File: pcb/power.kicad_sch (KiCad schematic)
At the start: 33 parts, among them J1 USB_C_PowerOnly_6P, J2 Power, J3 Power, U1 AZ1084-3.3, U2 LM66200DRLR

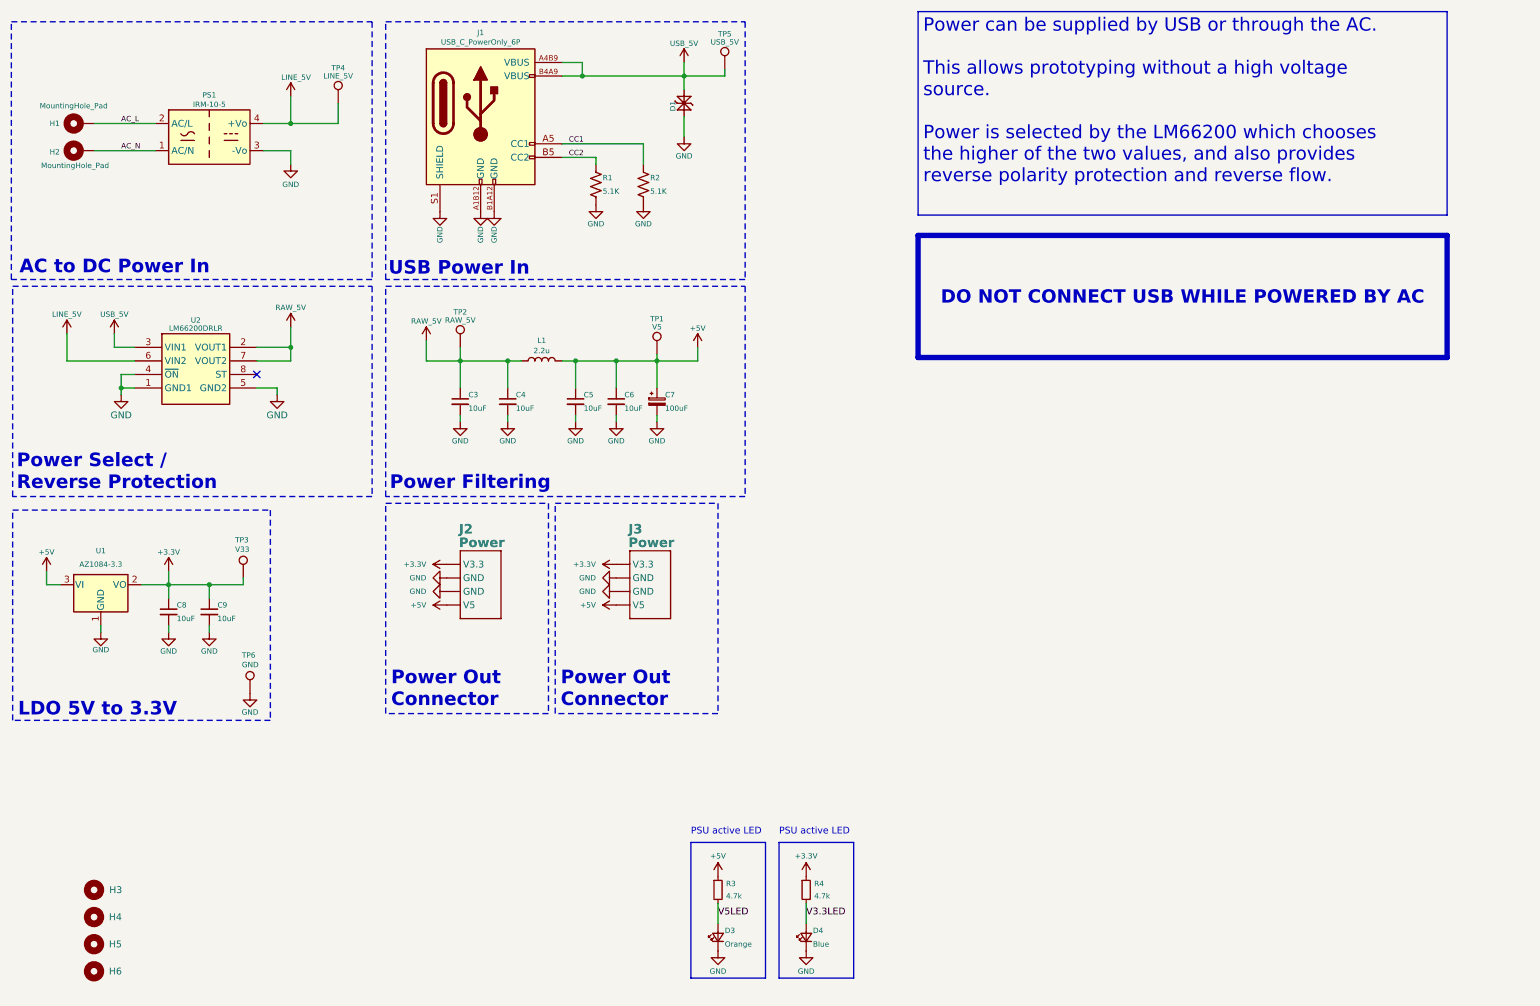
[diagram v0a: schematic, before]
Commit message: Added second power connector
Rearranged.
Added additional filtering
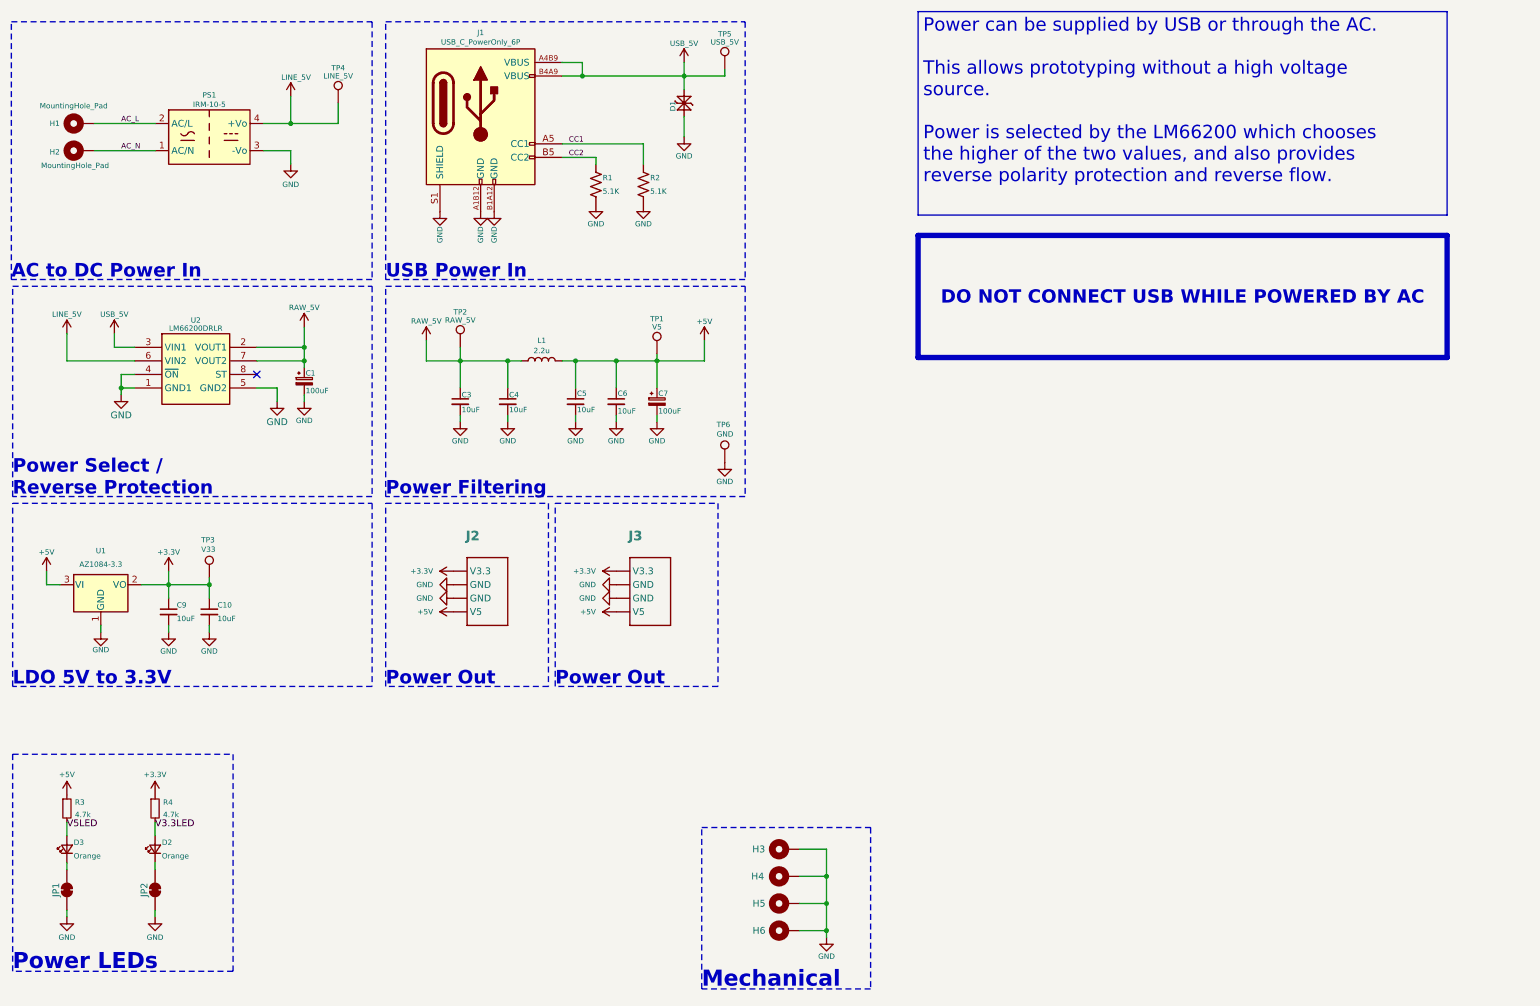
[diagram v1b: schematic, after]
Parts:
- removed D4: Blue, CRGM Passive:LED_0603_1608Metric, symbol Device:LED_Small
- added C1: 100uF, CRGM Passive:CP_Elec_6.3x5.4, symbol CRGM Passive:C_Polarized_Small
- added D2: Orange, CRGM Passive:LED_0603_1608Metric, symbol Device:LED_Small
- added JP1, JP2: ~, CRGM Connector:SolderJumper-2_P1.3mm_Bridged_RoundedPad1.0x1.5mm, symbol Jumper:SolderJumper_2_Bridged
- C10: renamed from C9; footprint Capacitor_SMD:C_0603_1608Metric -> CRGM Passive:C_0603_1608Metric
- C3, C4, C5, C6: footprint Capacitor_SMD:C_0603_1608Metric -> CRGM Passive:C_0603_1608Metric
- C7: footprint Capacitor_SMD:CP_Elec_6.3x7.7 -> CRGM Passive:CP_Elec_6.3x5.4; symbol Device:C_Polarized_Small -> CRGM Passive:C_Polarized_Small; Digikey 493-2203-2-ND -> PCE3866TR-ND; FT Rotation Offset 180 -> (none); Height (none) -> 5.4; LCSC C3339 -> C72474; MPN RVT1V101M0607 -> RVT1A101M0605; Mouser 647-UWT1V101MCL1S -> 667-EEE-1AA101SP; Notes 35V/Aluminum -> (none)
- C9: renamed from C8; footprint Capacitor_SMD:C_0603_1608Metric -> CRGM Passive:C_0603_1608Metric
- H3, H4, H5, H6: value MountingHole -> MountingHole_Pad; symbol Mechanical:MountingHole -> CRGM Mechanical:MountingHole_Pad
- J2, J3: value Power -> ~
- L1: footprint Inductor_SMD:L_Sunlord_MWSA0402S -> CRGM Passive:L_Sunlord_MWSA0402S
- R1, R2, R3, R4: footprint Resistor_SMD:R_0603_1608Metric -> CRGM Passive:R_0603_1608Metric
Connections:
- net GND: now also H3.1, H4.1, H5.1, H6.1, C1.2, JP1.1 (A), JP2.1 (A); no longer D3.1 (K)
- net RAW_5V: now also C1.1
- net V3.3LED: now also D2.2 (A)
- new net: D3.1 (K), JP1.2 (B)
- new net: D2.1 (K), JP2.2 (B)
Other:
- note added: "Mechanical"
- note added: "Power LEDs"
- note added: "Power Out"
- note removed: "PSU active LED"
- note removed: "Power Out Connector"
- moved on the sheet: J2, J3, R3, R4, TP3, TP6

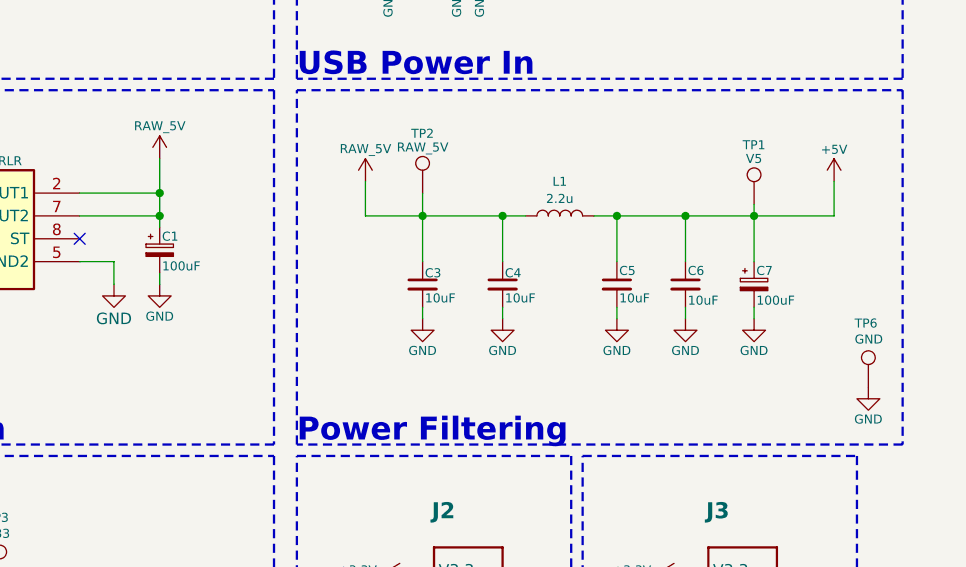
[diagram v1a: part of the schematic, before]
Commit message: Updated 100uF to 220uF
Adjusted part numbers
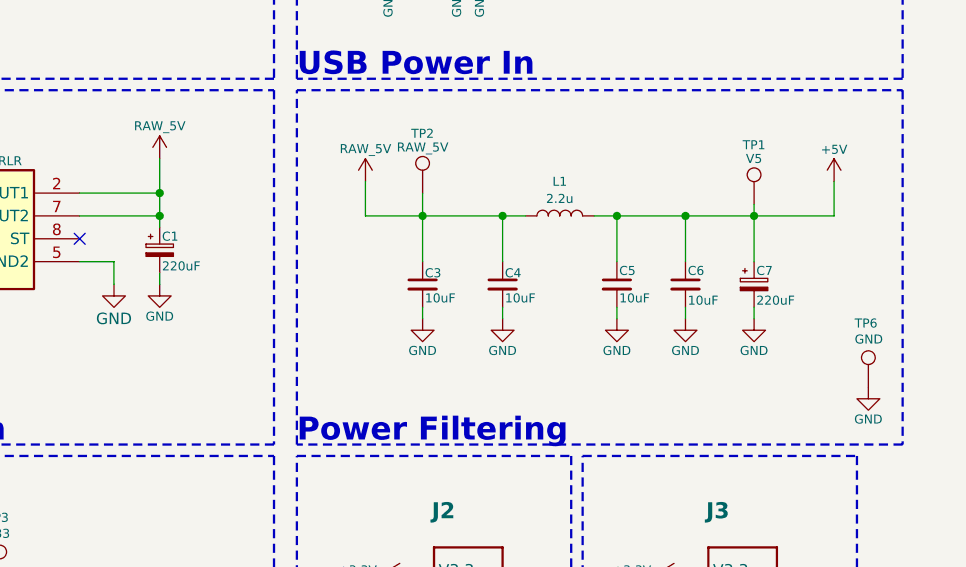
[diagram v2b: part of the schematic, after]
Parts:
- C1, C7: value 100uF -> 220uF; Digikey PCE3866TR-ND -> 3372-UE227M010HEHTATR-ND; LCSC C72474 -> C72494; MN Honor Elec -> ROQANG; MPN RVT1A101M0605 -> RVT1A221M0605; Mouser 667-EEE-1AA101SP -> 80-EDH227M6R3A9GAA
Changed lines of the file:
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@@
 	)
 	(symbol
+		(lib_id "CRGM Passive:C_Polarized_Small")
+		(at 69.85 82.55 0)
+		(unit 1)
+		(exclude_from_sim no)
+		(in_bom yes)
+		(on_board yes)
+		(dnp no)
+		(property "Reference" "C1"
+			(at 70.104 81.026 0)
+			(effects
+				(font
+					(size 1 1)
+				)
+				(justify left)
+			)
+		)
+		(property "Value" "220uF"
+			(at 70.104 84.328 0)
+			(effects
+				(font
+					(size 1 1)
+				)
+				(justify left)
+			)
+		)
+		(property "Footprint" "CRGM Passive:CP_Elec_6.3x5.4"
+			(at 69.85 82.55 0)
+			(effects
+				(font
+					(size 1.27 1.27)
+				)
+				(hide yes)
+			)
+		)
+		(property "Datasheet" "https://jlcpcb.com/api/file/downloadByFileSystemAccessId/8588885125476466688"
+			(at 69.85 82.55 0)
+			(effects
+				(font
+					(size 1.27 1.27)
+				)
+				(hide yes)
+			)
+		)
+		(property "Description" "-40℃~+105℃ 10V 2000hrs@105℃ 220uF 5.4mm 6.3mm 90mA@120Hz ±20%"
+			(at 69.85 92.71 0)
+			(effects
+				(font
+					(size 1.27 1.27)
+				)
+				(hide yes)
+			)
+		)
+		(property "MN" "ROQANG"
+			(at 69.85 82.55 0)
+			(effects
+				(font
+					(size 1.27 1.27)
+				)
+				(hide yes)
+			)
+		)
+		(property "MPN" "RVT1A221M0605"
+			(at 69.85 82.55 0)
+			(effects
+				(font
+					(size 1.27 1.27)
+				)
+				(hide yes)
+			)
+		)
+		(property "Mouser" "80-EDH227M6R3A9GAA"
+			(at 69.85 82.55 0)
+			(effects
+				(font
+					(size 1 1)
+					(color 223 129 255 1)
+				)
+				(hide yes)
+			)
+		)
+		(property "Digikey" "3372-UE227M010HEHTATR-ND"
+			(at 69.85 82.55 0)
+			(effects
+				(font
+					(size 1 1)
+					(color 223 129 255 1)
+				)
+				(hide yes)
+			)
+		)
+		(property "LCSC" "C72494"
+			(at 69.85 82.55 0)
+			(effects
+				(font
+					(size 1 1)
+					(color 223 129 255 1)
+				)
+				(hide yes)
+			)
+		)
+		(property "Height" "5.4"
+			(at 69.85 82.55 0)
+			(effects
+				(font
+					(size 1.27 1.27)
+				)
+				(hide yes)
+			)
+		)
+		(pin "1"
+		)
+		(pin "2"
+		)
+		(instances
+			(project "power-module"
+				(path "/445c1fff-2e1a-48b1-a91f-a137832edebf/cd8e8497-f5e1-4348-acdb-de9b8b105e95"
+					(reference "C1")
+					(unit 1)
+				)
+			)
+		)
+	)
+	(symbol
 		(lib_id "Device:R_Small")
 		(at 25.4 162.56 0)
@@
 			)
 		)
-		(property "Value" "100uF"
+		(property "Value" "220uF"
 			(at 136.144 88.138 0)
 			(effects
@@
 			)
 		)
-		(property "Datasheet" "~"
+		(property "Datasheet" "https://jlcpcb.com/api/file/downloadByFileSystemAccessId/8588885125476466688"
 			(at 135.89 86.36 0)
 			(effects
@@
 			)
 		)
-		(property "Description" "-40℃~+105℃ 100uF 10V 2000hrs@105℃ 5.4mm 55mA@120Hz 6.3mm ±20%"
+		(property "Description" "-40℃~+105℃ 10V 2000hrs@105℃ 220uF 5.4mm 6.3mm 90mA@120Hz ±20%"
 			(at 135.89 96.52 0)
 			(effects
@@
 			)
 		)
-		(property "MN" "Honor Elec"
+		(property "MN" "ROQANG"
 			(at 135.89 86.36 0)
 			(effects
@@
 			)
 		)
-		(property "MPN" "RVT1A101M0605"
+		(property "MPN" "RVT1A221M0605"
 			(at 135.89 86.36 0)
 			(effects
@@
 			)
 		)
-		(property "Mouser" "667-EEE-1AA101SP"
+		(property "Mouser" "80-EDH227M6R3A9GAA"
 			(at 135.89 86.36 0)
 			(effects
@@
 			)
 		)
-		(property "Digikey" "PCE3866TR-ND"
+		(property "Digikey" "3372-UE227M010HEHTATR-ND"
 			(at 135.89 86.36 0)
 			(effects
@@
 			)
 		)
-		(property "LCSC" "C72474"
+		(property "LCSC" "C72494"
 			(at 135.89 86.36 0)
 			(effects
@@
 			)
 		)
-		(property "Notes" ""
-			(at 135.89 86.36 0)
-			(effects
-				(font
-					(size 1.27 1.27)
-				)
-				(hide yes)
-			)
-		)
 		(pin "1"
 		)
@@
 					(unit 1)
 				)
-			)
-		)
-	)
-	(symbol
-		(lib_id "CRGM Passive:C_Polarized_Small")
-		(at 69.85 82.55 0)
-		(unit 1)
-		(exclude_from_sim no)
-		(in_bom yes)
-		(on_board yes)
-		(dnp no)
-		(property "Reference" "C1"
-			(at 70.104 81.026 0)
-			(effects
-				(font
-					(size 1 1)
-				)
-				(justify left)
-			)
-		)
-		(property "Value" "100uF"
-			(at 70.104 84.328 0)
-			(effects
-				(font
-					(size 1 1)
-				)
-				(justify left)
-			)
-		)
-		(property "Footprint" "CRGM Passive:CP_Elec_6.3x5.4"
-			(at 69.85 82.55 0)
-			(effects
-				(font
-					(size 1.27 1.27)
-				)
-				(hide yes)
-			)
-		)
-		(property "Datasheet" "~"
-			(at 69.85 82.55 0)
-			(effects
-				(font
-					(size 1.27 1.27)
-				)
-				(hide yes)
-			)
-		)
-		(property "Description" "-40℃~+105℃ 100uF 10V 2000hrs@105℃ 5.4mm 55mA@120Hz 6.3mm ±20%"
-			(at 69.85 92.71 0)
-			(effects
-				(font
-					(size 1.27 1.27)
-				)
-				(hide yes)
-			)
-		)
-		(property "MN" "Honor Elec"
-			(at 69.85 82.55 0)
-			(effects
-				(font
-					(size 1.27 1.27)
-				)
-				(hide yes)
-			)
-		)
-		(property "MPN" "RVT1A101M0605"
-			(at 69.85 82.55 0)
-			(effects
-				(font
-					(size 1.27 1.27)
-				)
-				(hide yes)
-			)
-		)
-		(property "Mouser" "667-EEE-1AA101SP"
-			(at 69.85 82.55 0)
-			(effects
-				(font
-					(size 1 1)
-					(color 223 129 255 1)
-				)
-				(hide yes)
-			)
-		)
-		(property "Digikey" "PCE3866TR-ND"
-			(at 69.85 82.55 0)
-			(effects
-				(font
-					(size 1 1)
-					(color 223 129 255 1)
-				)
-				(hide yes)
-			)
-		)
-		(property "LCSC" "C72474"
-			(at 69.85 82.55 0)
-			(effects
-				(font
-					(size 1 1)
-					(color 223 129 255 1)
-				)
-				(hide yes)
-			)
-		)
-		(property "Height" "5.4"
-			(at 69.85 82.55 0)
-			(effects
-				(font
-					(size 1.27 1.27)
-				)
-				(hide yes)
-			)
-		)
-		(property "Notes" ""
-			(at 69.85 82.55 0)
-			(effects
-				(font
-					(size 1.27 1.27)
-				)
-				(hide yes)
-			)
-		)
-		(pin "1"
-		)
-		(pin "2"
-		)
-		(instances
-			(project "power-module"
-				(path "/445c1fff-2e1a-48b1-a91f-a137832edebf/cd8e8497-f5e1-4348-acdb-de9b8b105e95"
-					(reference "C1")
-					(unit 1)
-				)
